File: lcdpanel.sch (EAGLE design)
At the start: 33 parts, among them J1 CHARLCD-LONG, SW1 PUSHSW, SW2 PUSHSW, SW3 PUSHSW, SW4 PUSHSW, X1 DCJACK-MJ179P-R

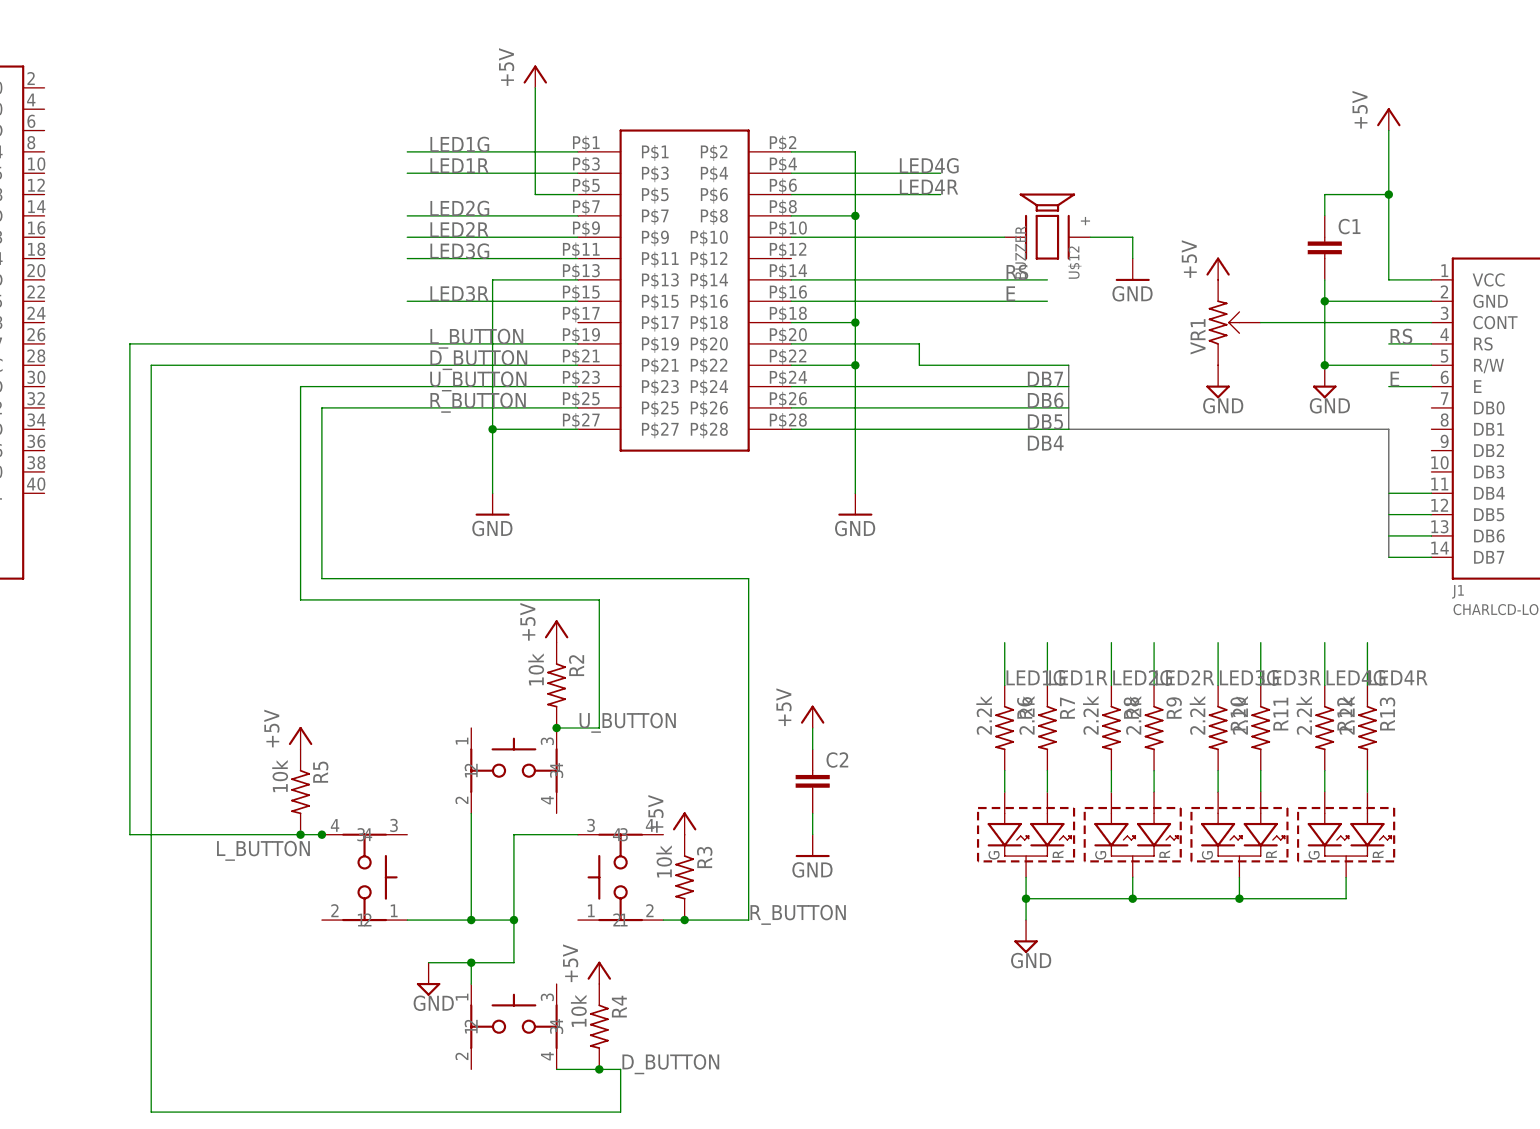
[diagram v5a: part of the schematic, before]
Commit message: fixed reversed connector on lcdpanel
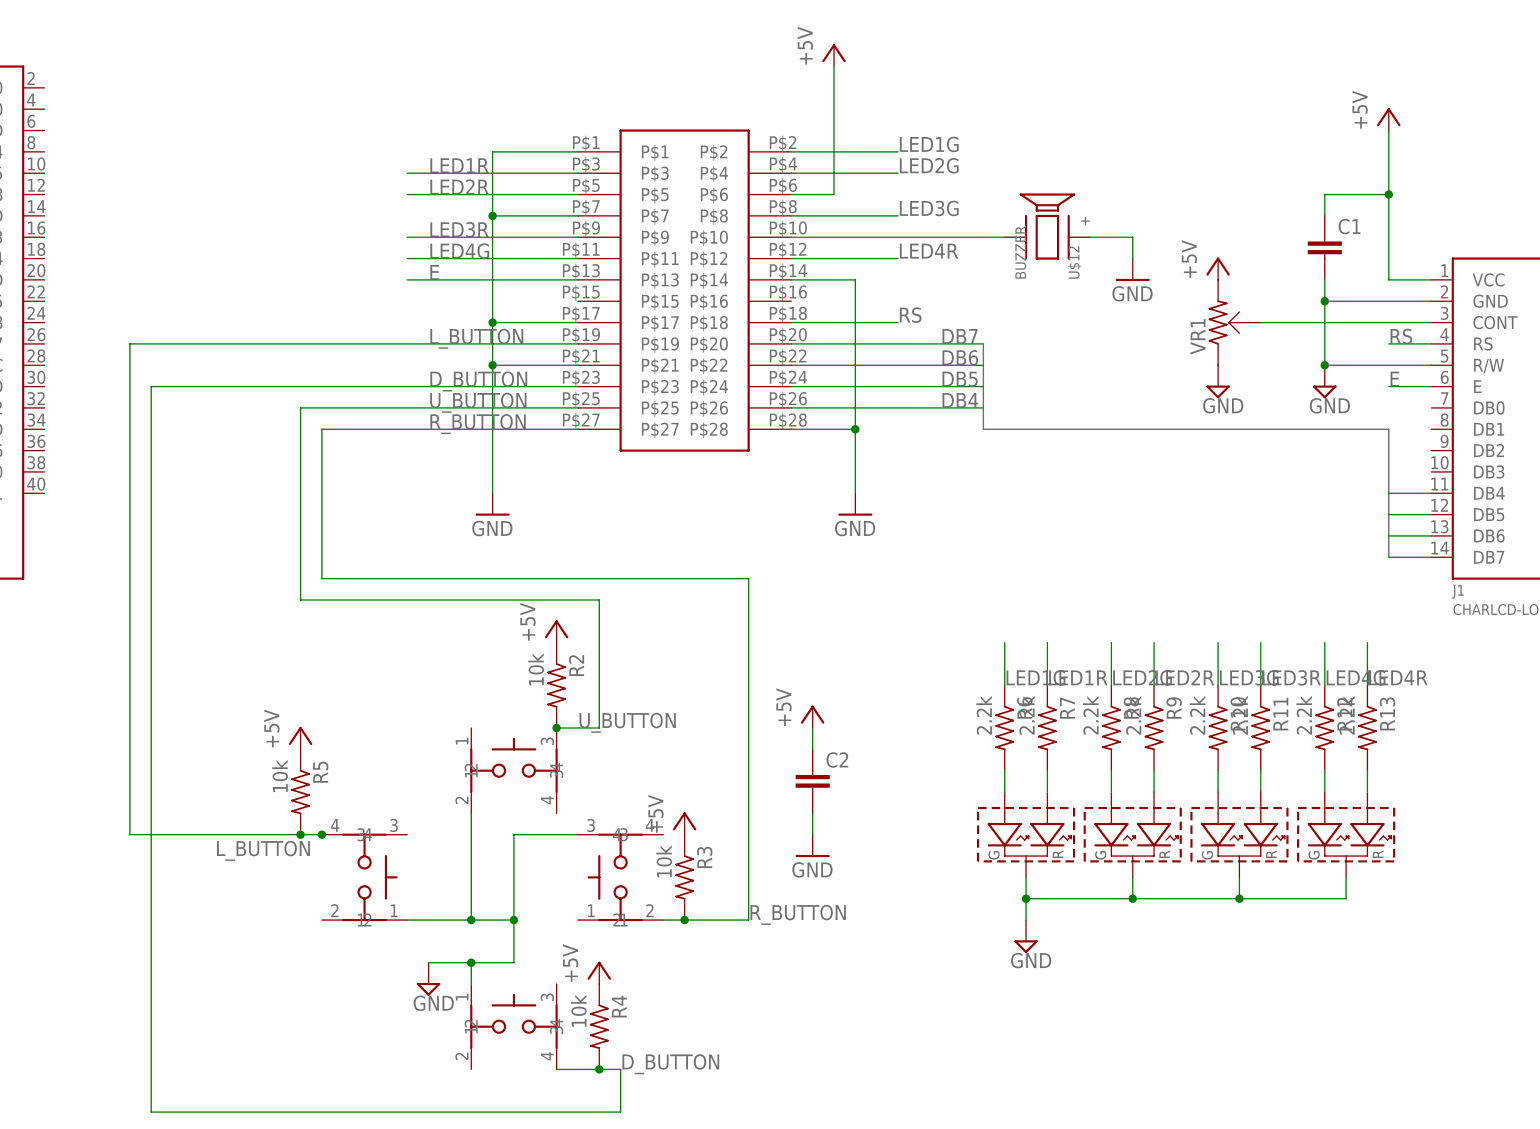
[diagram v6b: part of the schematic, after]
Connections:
- net +5V: now also U$13.P$6; no longer U$13.P$5
- net DB4: now also U$13.P$26; no longer U$13.P$28
- net DB5: now also U$13.P$24; no longer U$13.P$26
- net DB6: now also U$13.P$22; no longer U$13.P$24
- net D_BUTTON: now also U$13.P$23; no longer U$13.P$21
- net E: now also U$13.P$13; no longer U$13.P$16
- net GND: now also U$13.P$1, U$13.P$14, U$13.P$17, U$13.P$21, U$13.P$28, U$13.P$7; no longer U$13.P$13, U$13.P$18, U$13.P$2, U$13.P$22, U$13.P$27, U$13.P$8
- net LED1G: now also U$13.P$2; no longer U$13.P$1
- net LED2G: now also U$13.P$4; no longer U$13.P$7
- net LED2R: now also U$13.P$5; no longer U$13.P$9
- net LED3G: now also U$13.P$8; no longer U$13.P$11
- net LED3R: now also U$13.P$9; no longer U$13.P$15
- net LED4G: now also U$13.P$11; no longer U$13.P$4
- net LED4R: now also U$13.P$12; no longer U$13.P$6
- net RS: now also U$13.P$18; no longer U$13.P$14
- net R_BUTTON: now also U$13.P$27; no longer U$13.P$25
- net U_BUTTON: now also U$13.P$25; no longer U$13.P$23

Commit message: add AVR and bug fix
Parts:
- added C3: (no value), rcl:C-EUC0603
- added CON1: AVRISP-NEWSYMBOL-ML6, Connector_Robotech:AVRISP-NEWSYMBOL-ML6
- added R1: 10k, Passive_Robotech:R-1608
- added U1: ATTINY2313P, MicroControler_Robotech:ATTINY2313P
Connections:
- net R_BUTTON renamed MVO
- new net N$1: CON1RESET.S, R1.2, U1.RESET
- new net SCL: CON1SCK.S, U$13.P$2, U1.(USCK/SCL/PCINT7)PB7
- new net SDA: CON1MOSI.S, U$13.P$3, U1.(MOSI/DI/SDA/PCINT5)PB5
- net +5V: now also C3.1, CON1PWR.VCC, R1.1, U1.VCC
- net DB4: now also U1.(AIN0/PCINT0)PB0; no longer U$13.P$26
- net DB5: now also U1.(AIN1/PCINT1)PB1; no longer U$13.P$24
- net DB6: now also U1.(OC0A/PCINT2)PB2; no longer U$13.P$22
- net DB7: now also U1.(OC1A/PCINT3)PB3; no longer U$13.P$20
- net E: now also CON1MISO.S, U1.(MISO/DO/PCINT6)PB6; no longer U$13.P$13
- net GND: now also C3.2, CON1PWR.GND, U1.GND
- net LED1G: now also U1.(RXD)PD0; no longer U$13.P$2
- net LED1R: now also U1.(TXD)PD1; no longer U$13.P$3
- net LED2G: now also U1.(CKOUT/XCK/INT0)PD2; no longer U$13.P$4
- net LED2R: now also U1.(INT1)PD3; no longer U$13.P$5
- net LED3G: now also U1.(T0)PD4; no longer U$13.P$8
- net LED3R: now also U1.(OC0B/T1)PD5; no longer U$13.P$9
- net LED4G: now also U1.(ICP)PD6; no longer U$13.P$11
- net LED4R: now also U1.(OC1B/PCINT4)PB4; no longer U$13.P$12
- net N$2: now also U1.(XTAL1)PA0; no longer U$13.P$10
- net RS: now also U1.(XTAL2)PA1; no longer U$13.P$18
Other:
- moved on the sheet: C1, J1, R10, R11, R12, R13, R6, R7, R8, R9, U$11G$1, U$11G$2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
